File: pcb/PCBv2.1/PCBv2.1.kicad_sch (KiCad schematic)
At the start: 50 parts, among them J1 USB_C_Receptacle_USB2.0, J2 Conn_01x04, J3 Conn_01x04, J4 Conn_01x08, J5 Conn_01x08, SW1 SW_Push, SW2 SW_Push, U1 STM32F411CEUx, U2 BNO055, U3 AP2112K-3.3, Y1 32.768kHz, Y2 25MHz, Y3 32.768kHz

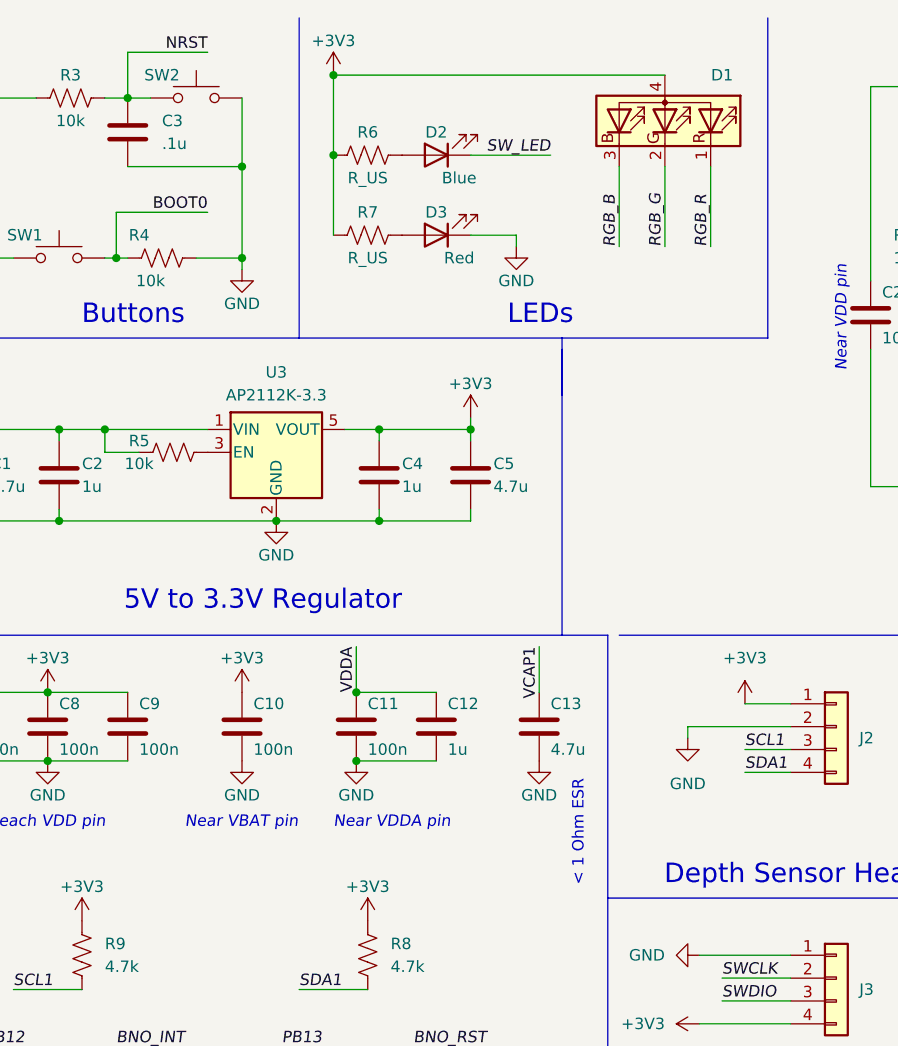
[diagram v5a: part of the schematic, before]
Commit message: Add more part numbers
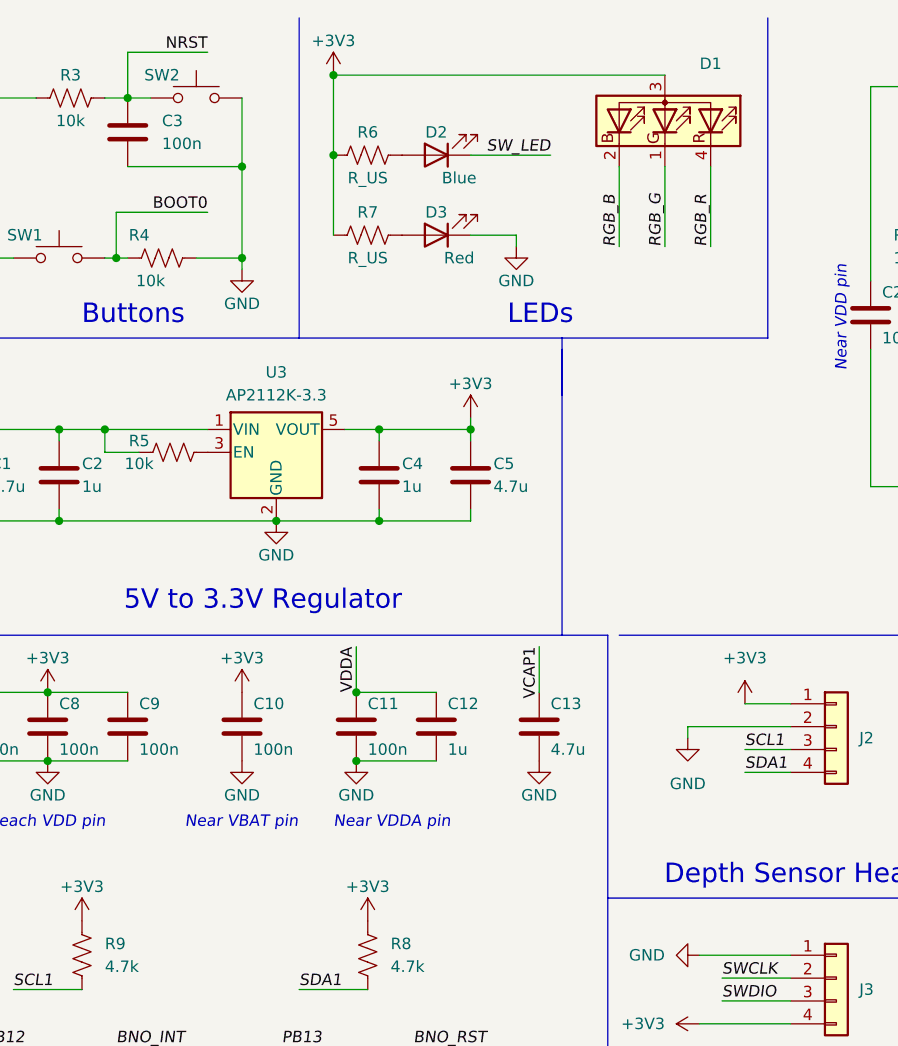
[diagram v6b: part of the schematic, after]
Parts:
- C1, C13, C5: footprint (none) -> Capacitor_SMD:C_0805_2012Metric_Pad1.18x1.45mm_HandSolder; Part Number (none) -> GRM21BC71E475KE11L
- C10, C11, C20, C7, C8, C9: footprint (none) -> Capacitor_SMD:C_0805_2012Metric_Pad1.18x1.45mm_HandSolder; Part Number (none) -> GCM21BR71E104JA37L
- C12, C2, C21, C4: footprint (none) -> Capacitor_SMD:C_0805_2012Metric_Pad1.18x1.45mm_HandSolder; Part Number (none) -> GCJ21BC72A105KE02L
- C14, C15, C18, C19: footprint (none) -> Capacitor_SMD:C_0805_2012Metric_Pad1.18x1.45mm_HandSolder; Part Number (none) -> GRM21A5C2E220FW01D
- C16, C17: footprint (none) -> Capacitor_SMD:C_0805_2012Metric_Pad1.18x1.45mm_HandSolder; Part Number (none) -> GQM2195C2E8R0CB12D
- C3: value .1u -> 100n; footprint (none) -> Capacitor_SMD:C_0805_2012Metric_Pad1.18x1.45mm_HandSolder; Part Number (none) -> GCM21BR71E104JA37L
- C6: footprint (none) -> Capacitor_SMD:C_0805_2012Metric_Pad1.18x1.45mm_HandSolder; Part Number (none) -> GRT21BC71E106KE13L
- D1: Part Number (none) -> QBL8RGB60D0-2897
- U1: Part Number (none) -> STM32F411CEU6
- U2: Part Number (none) -> BNO055
- U3: Part Number (none) -> AP2112K-3.3
- Y1, Y3: Part Number (none) -> ABS25-32.768KHZ-T
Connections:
- net +3V3: now also D1.3 (A); no longer D1.4 (A)
- net RGB_B: now also D1.2 (BK); no longer D1.3 (BK)
- net RGB_G: now also D1.1 (GK); no longer D1.2 (GK)
- net RGB_R: now also D1.4 (RK); no longer D1.1 (RK)
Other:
- note removed: "< 1 Ohm ESR"

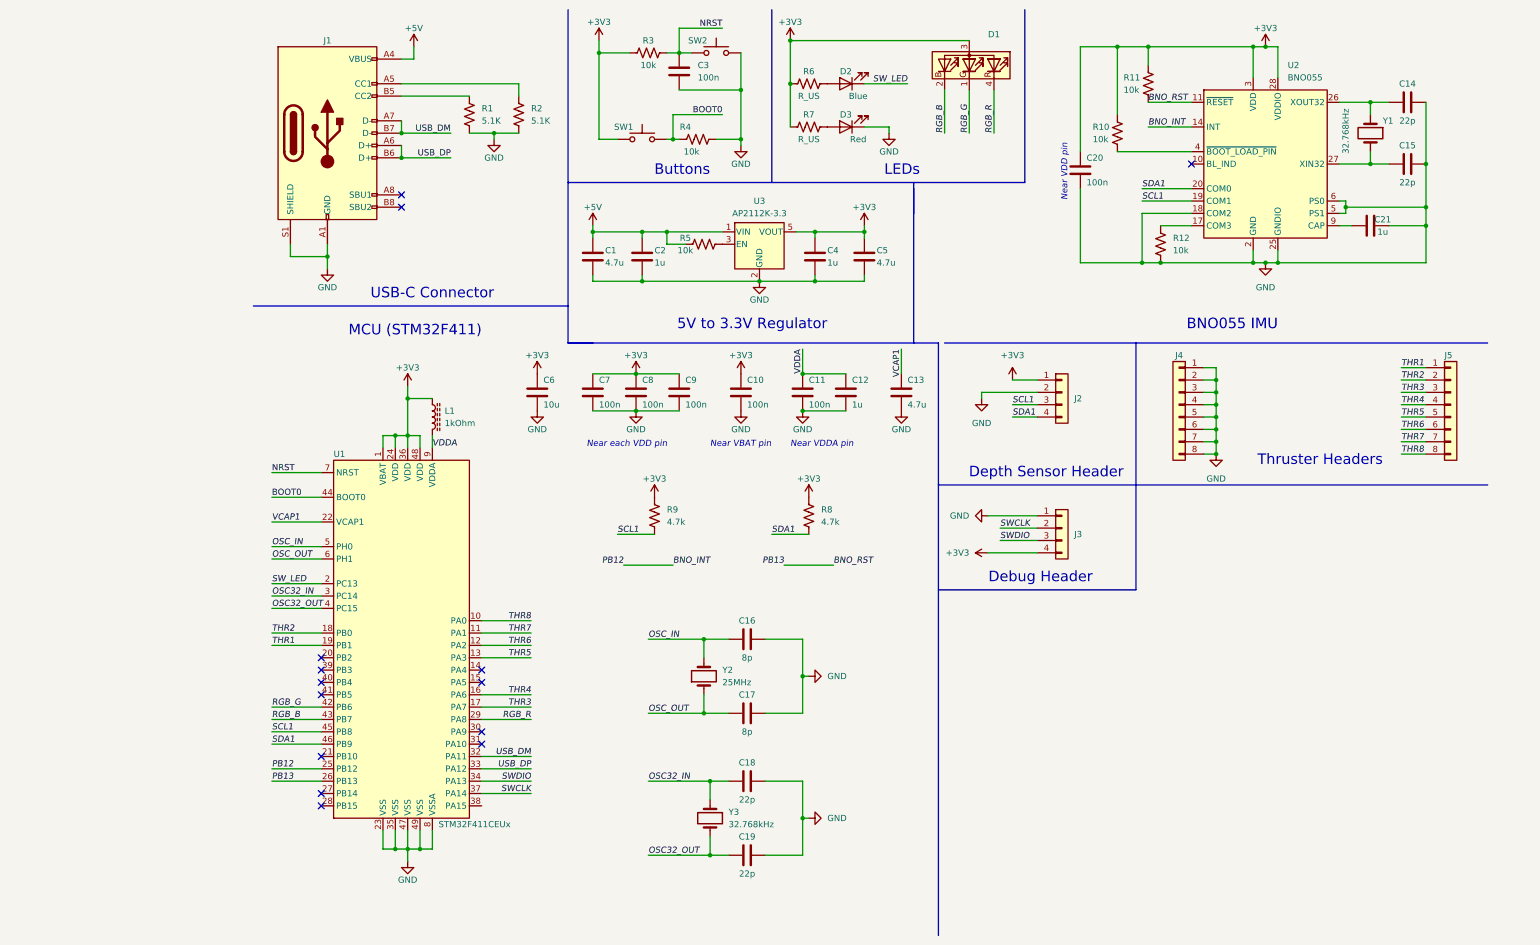
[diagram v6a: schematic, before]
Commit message: Add specific USB-C connector and resistor part numbers to pcb schematic
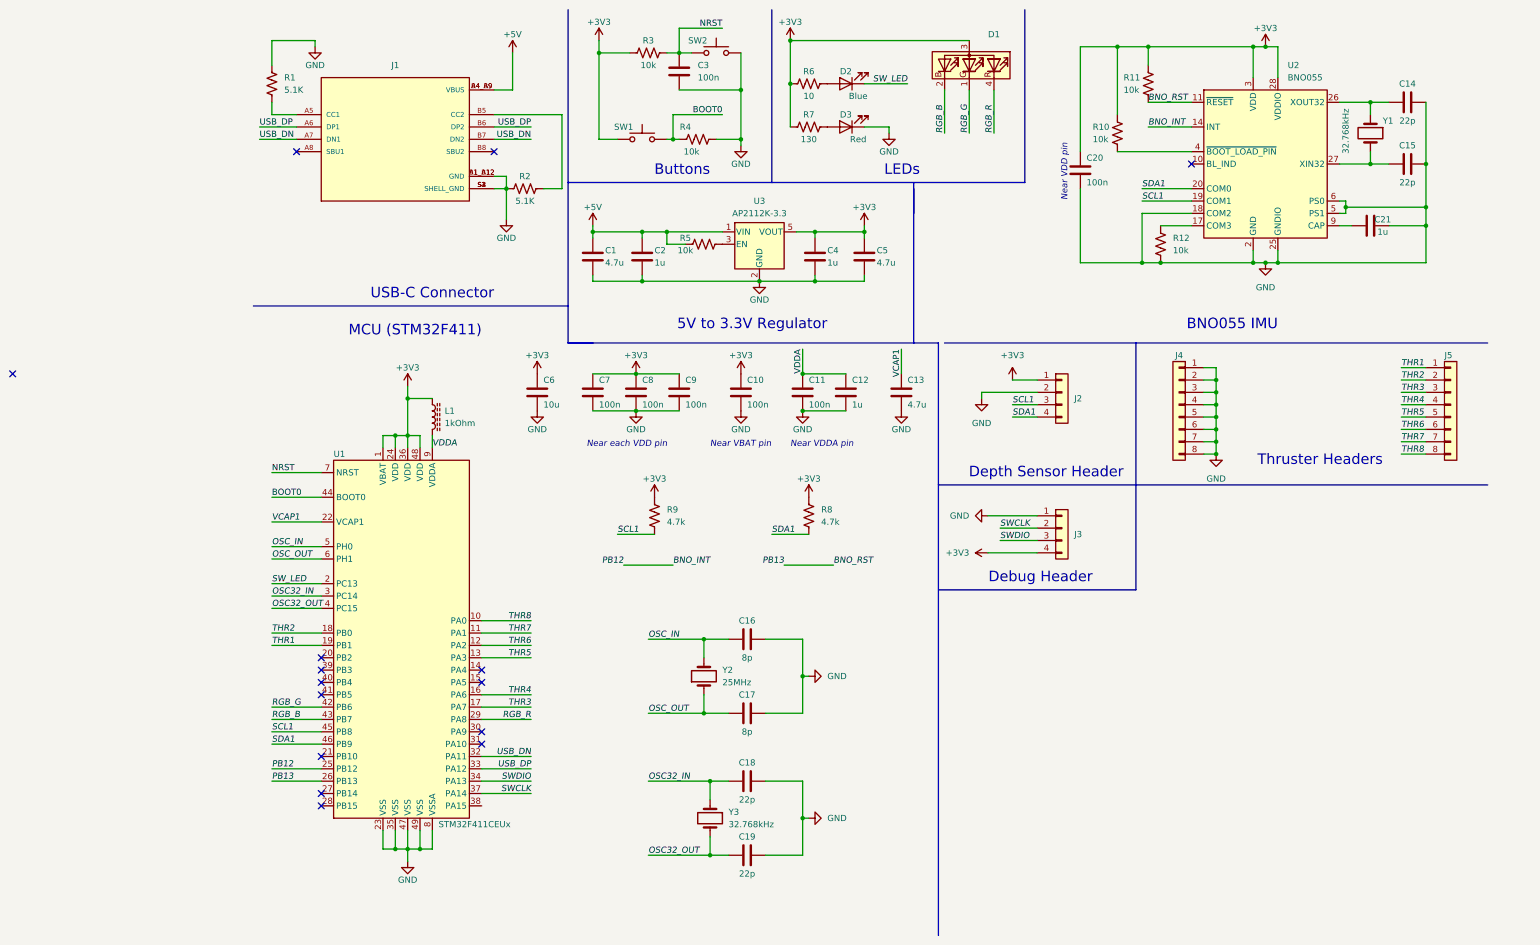
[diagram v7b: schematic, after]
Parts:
- removed J1: USB_C_Receptacle_USB2.0, symbol Connector:USB_C_Receptacle_USB2.0
- added J1: USB4105-GF-A, cboard:GCT_USB4105-GF-A, symbol cboard:USB4105-GF-A
- D2: footprint (none) -> LED_SMD:LED_0805_2012Metric_Pad1.15x1.40mm_HandSolder; Part Number (none) -> 150080BS75000
- D3: footprint (none) -> LED_SMD:LED_0805_2012Metric_Pad1.15x1.40mm_HandSolder; Part Number (none) -> 150080RS75000
- R1, R2: Part Number (none) -> ERJ-HP6F5101V
- R10, R11, R12, R3, R4, R5: Part Number (none) -> ERJ-6ENF1002V
- R6: value R_US -> 10; Part Number (none) -> ERJ-6ENF10R0V
- R7: value R_US -> 130; Part Number (none) -> ERJ-P06F1300V
- R8, R9: Part Number (none) -> ERJ-6ENF4701V
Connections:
- net +5V: now also J1.A4_B9 (VBUS), J1.B4_A9 (VBUS)
- net GND: now also R1.1, R2.1, J1.A1_B12 (GND), J1.B1_A12 (GND), J1.S1 (SHELL_GND), J1.S2 (SHELL_GND), J1.S3 (SHELL_GND), J1.S4 (SHELL_GND); no longer R1.2, R2.2
- net USB_DP: now also J1.A6 (DP1), J1.B6 (DP2)
- net USB_DM renamed USB_DN
- net USB_DN: now also J1.A7 (DN1), J1.B7 (DN2)
- new net: J1.B5 (CC2), R2.2
- new net: J1.A5 (CC1), R1.2
- no-connect marks 14 -> 15

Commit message: Add footprints for resistors
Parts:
- R1, R10, R11, R12, R2, R3, R4, R5, R6, R7, R8, R9: footprint (none) -> Resistor_SMD:R_0805_2012Metric_Pad1.20x1.40mm_HandSolder
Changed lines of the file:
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@@
     (property "Reference" "R4" (id 0) (at 101.6 36.83 90))
     (property "Value" "10k" (id 1) (at 102.87 41.91 90))
-    (property "Footprint" "" (id 2) (at 104.394 38.354 90)
+    (property "Footprint" "Resistor_SMD:R_0805_2012Metric_Pad1.20x1.40mm_HandSolder" (id 2) (at 104.394 38.354 90)
       (effects (font (size 1.27 1.27)) hide)
     )
@@
     (property "Reference" "R2" (id 0) (at 68.58 46.99 90))
     (property "Value" "5.1K" (id 1) (at 68.58 52.07 90))
-    (property "Footprint" "" (id 2) (at 68.834 48.514 90)
+    (property "Footprint" "Resistor_SMD:R_0805_2012Metric_Pad1.20x1.40mm_HandSolder" (id 2) (at 68.834 48.514 90)
       (effects (font (size 1.27 1.27)) hide)
     )
@@
       (effects (font (size 1.27 1.27)) (justify left))
     )
-    (property "Footprint" "" (id 2) (at 96.266 117.094 90)
+    (property "Footprint" "Resistor_SMD:R_0805_2012Metric_Pad1.20x1.40mm_HandSolder" (id 2) (at 96.266 117.094 90)
       (effects (font (size 1.27 1.27)) hide)
     )
@@
       (effects (font (size 1.27 1.27)) (justify left))
     )
-    (property "Footprint" "" (id 2) (at 128.016 117.094 90)
+    (property "Footprint" "Resistor_SMD:R_0805_2012Metric_Pad1.20x1.40mm_HandSolder" (id 2) (at 128.016 117.094 90)
       (effects (font (size 1.27 1.27)) hide)
     )
@@
     (property "Reference" "R6" (id 0) (at 127 25.4 90))
     (property "Value" "10" (id 1) (at 127 30.48 90))
-    (property "Footprint" "" (id 2) (at 127.254 26.924 90)
+    (property "Footprint" "Resistor_SMD:R_0805_2012Metric_Pad1.20x1.40mm_HandSolder" (id 2) (at 127.254 26.924 90)
       (effects (font (size 1.27 1.27)) hide)
     )
@@
       (effects (font (size 1.27 1.27)) (justify left))
     )
-    (property "Footprint" "" (id 2) (at 197.866 28.194 90)
+    (property "Footprint" "Resistor_SMD:R_0805_2012Metric_Pad1.20x1.40mm_HandSolder" (id 2) (at 197.866 28.194 90)
       (effects (font (size 1.27 1.27)) hide)
     )
@@
       (effects (font (size 1.27 1.27)) (justify left))
     )
-    (property "Footprint" "" (id 2) (at 200.406 61.214 90)
+    (property "Footprint" "Resistor_SMD:R_0805_2012Metric_Pad1.20x1.40mm_HandSolder" (id 2) (at 200.406 61.214 90)
       (effects (font (size 1.27 1.27)) hide)
     )
@@
     (property "Reference" "R7" (id 0) (at 127 34.29 90))
     (property "Value" "130" (id 1) (at 127 39.37 90))
-    (property "Footprint" "" (id 2) (at 127.254 35.814 90)
+    (property "Footprint" "Resistor_SMD:R_0805_2012Metric_Pad1.20x1.40mm_HandSolder" (id 2) (at 127.254 35.814 90)
       (effects (font (size 1.27 1.27)) hide)
     )
@@
     (property "Reference" "R5" (id 0) (at 101.6 59.69 90))
     (property "Value" "10k" (id 1) (at 101.6 62.23 90))
-    (property "Footprint" "" (id 2) (at 105.664 59.944 90)
+    (property "Footprint" "Resistor_SMD:R_0805_2012Metric_Pad1.20x1.40mm_HandSolder" (id 2) (at 105.664 59.944 90)
       (effects (font (size 1.27 1.27)) hide)
     )
@@
     (property "Reference" "R3" (id 0) (at 93.98 19.05 90))
     (property "Value" "10k" (id 1) (at 93.98 24.13 90))
-    (property "Footprint" "" (id 2) (at 94.234 20.574 90)
+    (property "Footprint" "Resistor_SMD:R_0805_2012Metric_Pad1.20x1.40mm_HandSolder" (id 2) (at 94.234 20.574 90)
       (effects (font (size 1.27 1.27)) hide)
     )
@@
       (effects (font (size 1.27 1.27)) (justify left))
     )
-    (property "Footprint" "" (id 2) (at 191.516 38.354 90)
+    (property "Footprint" "Resistor_SMD:R_0805_2012Metric_Pad1.20x1.40mm_HandSolder" (id 2) (at 191.516 38.354 90)
       (effects (font (size 1.27 1.27)) hide)
     )
@@
       (effects (font (size 1.27 1.27)) (justify left))
     )
-    (property "Footprint" "" (id 2) (at 17.526 28.194 90)
+    (property "Footprint" "Resistor_SMD:R_0805_2012Metric_Pad1.20x1.40mm_HandSolder" (id 2) (at 17.526 28.194 90)
       (effects (font (size 1.27 1.27)) hide)
     )
@@
     )
     (path "/ed367056-76af-4d12-afed-c14ed9ea3e62"
-      (reference "R1") (unit 1) (value "5.1K") (footprint "")
+      (reference "R1") (unit 1) (value "5.1K") (footprint "Resistor_SMD:R_0805_2012Metric_Pad1.20x1.40mm_HandSolder")
     )
     (path "/1ca47c9e-e89f-4da3-acb5-819626522672"
-      (reference "R2") (unit 1) (value "5.1K") (footprint "")
+      (reference "R2") (unit 1) (value "5.1K") (footprint "Resistor_SMD:R_0805_2012Metric_Pad1.20x1.40mm_HandSolder")
     )
     (path "/e4d86865-a516-4521-88cd-ce68c78255e8"
-      (reference "R3") (unit 1) (value "10k") (footprint "")
+      (reference "R3") (unit 1) (value "10k") (footprint "Resistor_SMD:R_0805_2012Metric_Pad1.20x1.40mm_HandSolder")
     )
     (path "/082c5799-c4fd-4ab4-8c8f-1014f24c979f"
-      (reference "R4") (unit 1) (value "10k") (footprint "")
+      (reference "R4") (unit 1) (value "10k") (footprint "Resistor_SMD:R_0805_2012Metric_Pad1.20x1.40mm_HandSolder")
     )
     (path "/cbc75471-8141-4cfc-8762-2fd42b2764b4"
-      (reference "R5") (unit 1) (value "10k") (footprint "")
+      (reference "R5") (unit 1) (value "10k") (footprint "Resistor_SMD:R_0805_2012Metric_Pad1.20x1.40mm_HandSolder")
     )
     (path "/5ecd738d-80a3-4c45-92d6-6ed50e36bff7"
-      (reference "R6") (unit 1) (value "10") (footprint "")
+      (reference "R6") (unit 1) (value "10") (footprint "Resistor_SMD:R_0805_2012Metric_Pad1.20x1.40mm_HandSolder")
     )
     (path "/901c9e94-a57e-4f5b-9a33-2edb1ad2af4a"
-      (reference "R7") (unit 1) (value "130") (footprint "")
+      (reference "R7") (unit 1) (value "130") (footprint "Resistor_SMD:R_0805_2012Metric_Pad1.20x1.40mm_HandSolder")
     )
     (path "/51439732-d366-4779-9440-e9891544139c"
-      (reference "R8") (unit 1) (value "4.7k") (footprint "")
+      (reference "R8") (unit 1) (value "4.7k") (footprint "Resistor_SMD:R_0805_2012Metric_Pad1.20x1.40mm_HandSolder")
     )
     (path "/4e797149-dfa4-4a50-b439-f34510a1f5cf"
-      (reference "R9") (unit 1) (value "4.7k") (footprint "")
+      (reference "R9") (unit 1) (value "4.7k") (footprint "Resistor_SMD:R_0805_2012Metric_Pad1.20x1.40mm_HandSolder")
     )
     (path "/e8538eb1-4435-4516-a184-2646c420ea95"
-      (reference "R10") (unit 1) (value "10k") (footprint "")
+      (reference "R10") (unit 1) (value "10k") (footprint "Resistor_SMD:R_0805_2012Metric_Pad1.20x1.40mm_HandSolder")
     )
     (path "/6c763305-9ebb-4993-b12d-a59a6a5e39fd"
-      (reference "R11") (unit 1) (value "10k") (footprint "")
+      (reference "R11") (unit 1) (value "10k") (footprint "Resistor_SMD:R_0805_2012Metric_Pad1.20x1.40mm_HandSolder")
     )
     (path "/7522f90f-733e-4f07-8c2f-aad74a0f7633"
-      (reference "R12") (unit 1) (value "10k") (footprint "")
+      (reference "R12") (unit 1) (value "10k") (footprint "Resistor_SMD:R_0805_2012Metric_Pad1.20x1.40mm_HandSolder")
     )
     (path "/833c6f12-9e24-43f0-b3a0-e54ccab04f6f"
